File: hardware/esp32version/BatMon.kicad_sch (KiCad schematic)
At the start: 33 parts, among them J1 Battery_Connector, J3 Prog_Connector, J5 Charging_Connector, Q1 Q_PMOS_DDGSDD_TSOP-6, Q2 Q_PMOS_DDGSDD_TSOP-6, Q3 SS8050-G, SW1 POWER_SW, U1 ESP32-WROOM-32D, U2 LM2904, U4 AZ1117CR-3.3

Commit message: finalized design and exported gerbers
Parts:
- added C6: 22µ, Capacitor_Tantalum_SMD:CP_EIA-3216-18_Kemet-A_Pad1.58x1.35mm_HandSolder, symbol Device:C_Polarized
- added Q1, Q2: SS8050-G, Package_TO_SOT_SMD:SOT-23, symbol ELEKTRON_Components:SS8050-G
- added R2, R3: 10k, Resistor_SMD:R_0603_1608Metric_Pad0.98x0.95mm_HandSolder, symbol Device:R
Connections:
- net GND: now also C6.2
- net ESP_EN: now reaches R10.1, U1.3 (EN)
- net ESP_EN: now also C6.1, Q1.3 (C); no longer J3.1 (Pin_1)
- net ESP_IO0: now reaches U1.25 (IO0)
- net ESP_IO0: now also Q2.3 (C); no longer J3.2 (Pin_2)
- net RXD: now reaches J3.4 (Pin_4), U1.34 (RXD0/IO3)
- net TXD: now reaches J3.3 (Pin_3), U1.35 (TXD0/IO1)
- new net: Q1.1 (B), R2.1
- new net: Q2.1 (B), R3.1
- new net PROG_DTR: J3.2 (Pin_2), Q2.2 (E), R2.2
- new net PROG_RTS: J3.1 (Pin_1), Q1.2 (E), R3.2
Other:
- note added: "Reset Circuitry"
- moved on the sheet: R10

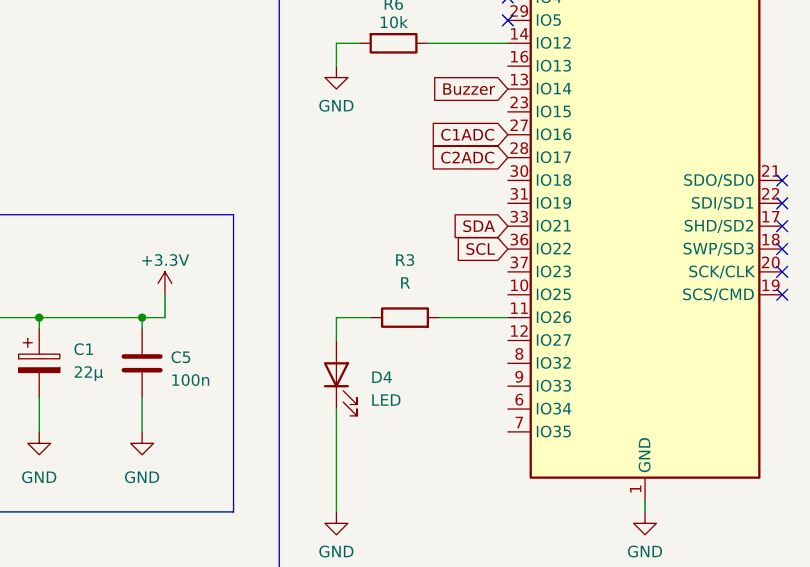
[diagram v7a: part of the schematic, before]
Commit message: added part fields and bom
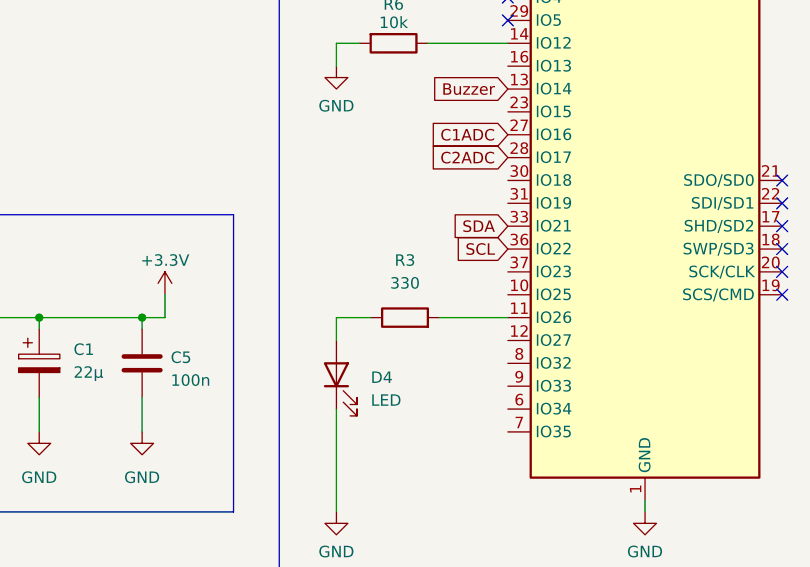
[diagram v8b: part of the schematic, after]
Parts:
- BZ1: Part (none) -> https://www.mouser.at/ProductDetail/CUI-Devices/CMT-85853-9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
- C1, C2, C6: Part (none) -> https://www.mouser.at/ProductDetail/KEMET/T491A226K010AT?qs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
- C3, C4, C5: Part (none) -> https://www.mouser.at/ProductDetail/KEMET/C0603C104K5RAC312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
- D1, D2: Part (none) -> https://www.mouser.at/ProductDetail/Vishay-Semiconductors/M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
- D3: Part (none) -> https://www.mouser.at/ProductDetail/Nexperia/PMEG4030ETRX?q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
- D4: Part (none) -> https://www.mouser.at/ProductDetail/ROHM-Semiconductor/SML-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
- D5: Part (none) -> https://www.mouser.at/ProductDetail/Bourns/CG1206MLC-12E?qs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
- J1: Part (none) -> https://www.reichelt.at/at/de/jst-stiftleiste-90-1x3-polig-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
- J3: Part (none) -> https://www.mouser.at/ProductDetail/Harwin/M50-3930542?qs=%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
- J5: Part (none) -> https://www.mouser.at/ProductDetail/TE-Connectivity-AMP/3-8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; Receptacle https://www.mouser.at/ProductDetail/TE-Connectivity-AMP/3-8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 -> (none)
- Q1, Q2: Part (none) -> https://www.mouser.at/ProductDetail/Vishay-Siliconix/SI3483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
- Q1, Q2, Q3: Part (none) -> https://www.mouser.at/ProductDetail/Comchip-Technology/SS80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
- R1, R11: Part (none) -> https://www.mouser.at/ProductDetail/Panasonic/ERJ-3GEYJ303V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
- R10, R12, R2, R3, R4, R6: Part (none) -> https://www.mouser.at/ProductDetail/Panasonic/ERJ-3GEYJ103V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
- R3: value R -> 330; Part (none) -> https://www.mouser.at/ProductDetail/Panasonic/ERJ-3GEYJ331V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
- R5, R7, R8: Part (none) -> https://www.mouser.at/ProductDetail/Panasonic/ERJ-3GEYJ331V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
- R9: Part (none) -> https://www.mouser.at/ProductDetail/Panasonic/ERJ-3GEYJ203V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
- SW1: Part (none) -> https://www.mouser.at/ProductDetail/Nidec-Components/CL-SB-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
- U1: Part (none) -> https://www.mouser.at/ProductDetail/Espressif-Systems/ESP32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
- U2: Part (none) -> https://www.mouser.at/ProductDetail/Texas-Instruments/LM290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
- U2: footprint (none) -> Package_SO:SOIC-8_3.9x4.9mm_P1.27mm; Part (none) -> https://www.mouser.at/ProductDetail/Texas-Instruments/LM290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
- U4: Part (none) -> https://www.mouser.at/ProductDetail/Diodes-Incorporated/AZ1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
